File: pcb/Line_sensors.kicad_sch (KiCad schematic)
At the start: 23 parts, among them Q5 BC817, U10 CNY70, U11 CNY70, U5 CNY70, U6 CNY70, U7 CNY70, U8 CNY70, U9 CNY70

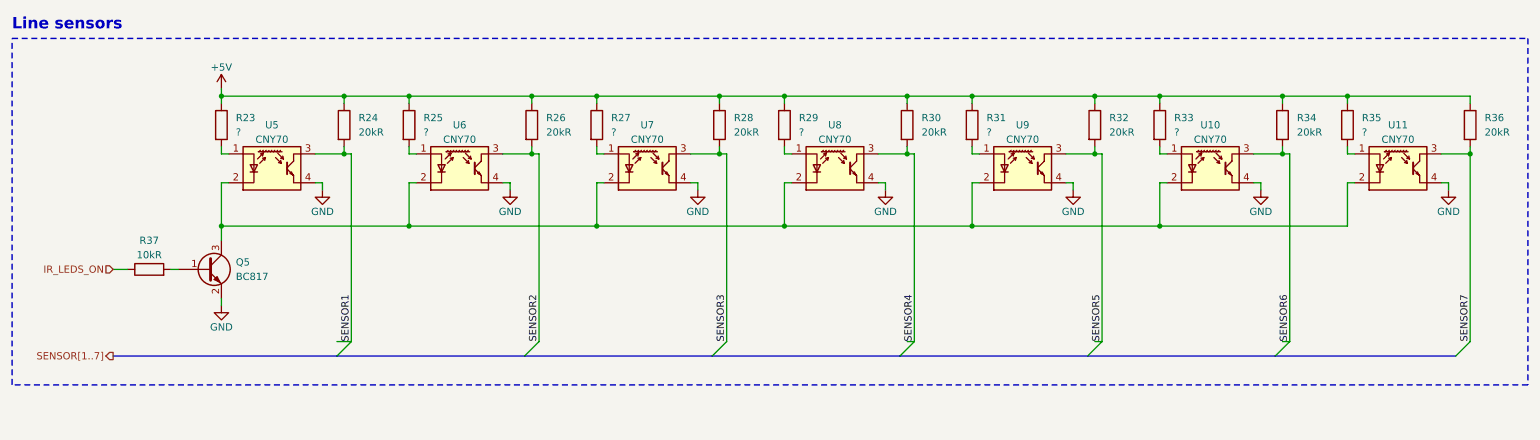
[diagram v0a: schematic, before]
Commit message: [pcb] Test point added
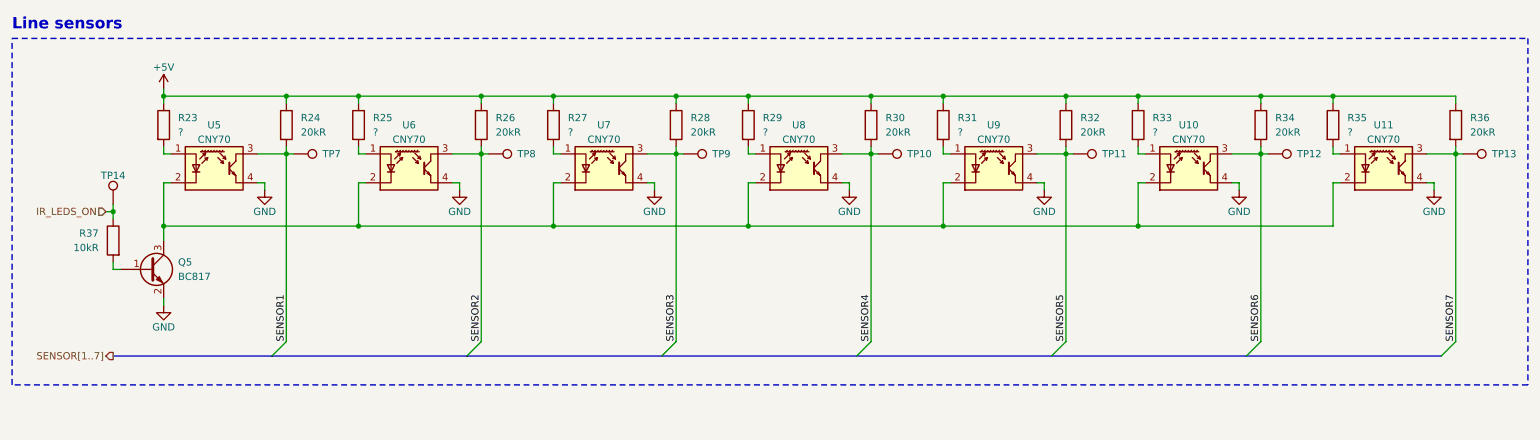
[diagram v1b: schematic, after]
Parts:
- added TP10, TP11, TP12, TP13, TP14, TP7, TP8, TP9: TestPoint, symbol Connector:TestPoint
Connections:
- net IR_LEDS_ON: now also TP14.1
- net SENSOR1: now also TP7.1
- net SENSOR2: now also TP8.1
- net SENSOR3: now also TP9.1
- net SENSOR4: now also TP10.1
- net SENSOR5: now also TP11.1
- net SENSOR6: now also TP12.1
- net SENSOR7: now also TP13.1
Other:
- moved on the sheet: Q5, R23, R24, R25, R26, R27, R28, R29, R30, R31, R32, R33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

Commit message: [pcb] Schematic clean-up
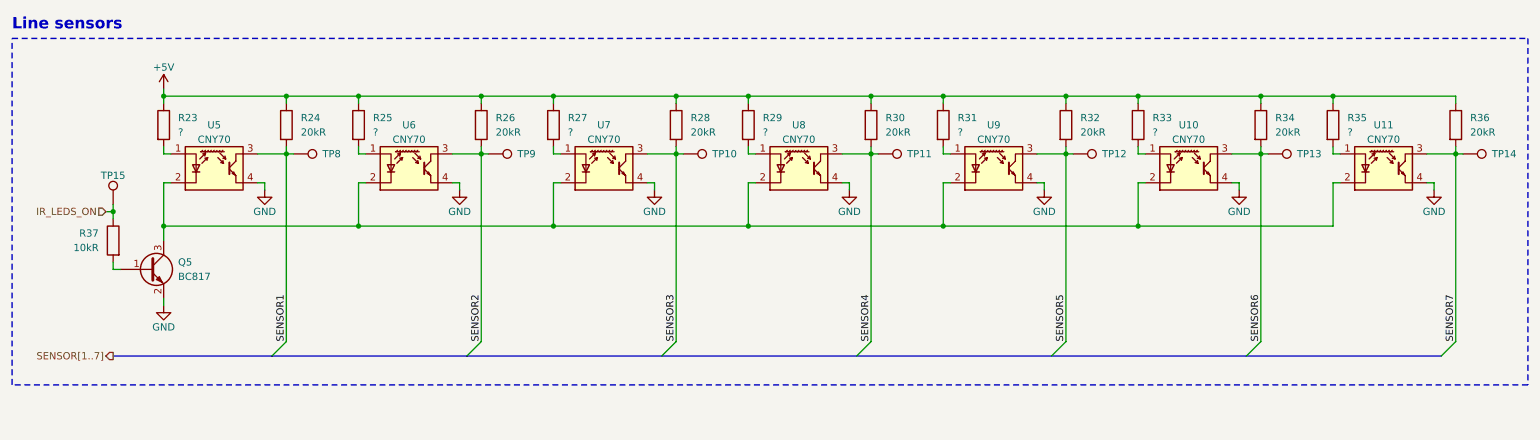
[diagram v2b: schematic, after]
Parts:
- renumbered TP9 to TP10, TP10 to TP11, TP11 to TP12, TP12 to TP13, TP13 to TP14, TP14 to TP15, TP7 to TP8, TP8 to TP9
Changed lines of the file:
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@@
   (symbol (lib_id "Connector:TestPoint") (at 236.22 39.37 270) (unit 1)
     (in_bom yes) (on_board yes) (dnp no)
-    (property "Reference" "TP12" (at 241.3 39.37 90)
+    (property "Reference" "TP13" (at 241.3 39.37 90)
       (effects (font (size 1.27 1.27)) (justify left))
     )
@@
       (project "Autko"
         (path "/8d5cfdec-de34-4148-9100-7125640c46f5/80d635c6-4a73-4538-989a-c930c6a7f33b"
-          (reference "TP12") (unit 1)
+          (reference "TP13") (unit 1)
         )
       )
@@
   (symbol (lib_id "Connector:TestPoint") (at 133.35 39.37 270) (unit 1)
     (in_bom yes) (on_board yes) (dnp no)
-    (property "Reference" "TP9" (at 138.43 39.37 90)
+    (property "Reference" "TP10" (at 138.43 39.37 90)
       (effects (font (size 1.27 1.27)) (justify left))
     )
@@
       (project "Autko"
         (path "/8d5cfdec-de34-4148-9100-7125640c46f5/80d635c6-4a73-4538-989a-c930c6a7f33b"
+          (reference "TP10") (unit 1)
+        )
+      )
+    )
+  )
+  (symbol (lib_id "Connector:TestPoint") (at 99.06 39.37 270) (unit 1)
+    (in_bom yes) (on_board yes) (dnp no)
+    (property "Reference" "TP9" (at 104.14 39.37 90)
+      (effects (font (size 1.27 1.27)) (justify left))
+    )
+    (property "Value" "TestPoint" (at 104.14 41.275 90)
+      (effects (font (size 1.27 1.27)) (justify left) hide)
+    )
+    (property "Footprint" "" (at 99.06 44.45 0)
+      (effects (font (size 1.27 1.27)) hide)
+    )
+    (property "Datasheet" "~" (at 99.06 44.45 0)
+      (effects (font (size 1.27 1.27)) hide)
+    )
+    (pin "1")
+    (instances
+      (project "Autko"
+        (path "/8d5cfdec-de34-4148-9100-7125640c46f5/80d635c6-4a73-4538-989a-c930c6a7f33b"
           (reference "TP9") (unit 1)
-        )
-      )
-    )
-  )
-  (symbol (lib_id "Connector:TestPoint") (at 99.06 39.37 270) (unit 1)
-    (in_bom yes) (on_board yes) (dnp no)
-    (property "Reference" "TP8" (at 104.14 39.37 90)
-      (effects (font (size 1.27 1.27)) (justify left))
-    )
-    (property "Value" "TestPoint" (at 104.14 41.275 90)
-      (effects (font (size 1.27 1.27)) (justify left) hide)
-    )
-    (property "Footprint" "" (at 99.06 44.45 0)
-      (effects (font (size 1.27 1.27)) hide)
-    )
-    (property "Datasheet" "~" (at 99.06 44.45 0)
-      (effects (font (size 1.27 1.27)) hide)
-    )
-    (pin "1")
-    (instances
-      (project "Autko"
-        (path "/8d5cfdec-de34-4148-9100-7125640c46f5/80d635c6-4a73-4538-989a-c930c6a7f33b"
-          (reference "TP8") (unit 1)
         )
       )
@@
   (symbol (lib_id "Connector:TestPoint") (at 201.93 39.37 270) (unit 1)
     (in_bom yes) (on_board yes) (dnp no)
-    (property "Reference" "TP11" (at 207.01 39.37 90)
+    (property "Reference" "TP12" (at 207.01 39.37 90)
       (effects (font (size 1.27 1.27)) (justify left))
     )
@@
       (project "Autko"
         (path "/8d5cfdec-de34-4148-9100-7125640c46f5/80d635c6-4a73-4538-989a-c930c6a7f33b"
-          (reference "TP11") (unit 1)
+          (reference "TP12") (unit 1)
         )
       )
@@
   (symbol (lib_id "Connector:TestPoint") (at 33.02 48.26 0) (unit 1)
     (in_bom yes) (on_board yes) (dnp no)
-    (property "Reference" "TP14" (at 33.02 43.18 0)
+    (property "Reference" "TP15" (at 33.02 43.18 0)
       (effects (font (size 1.27 1.27)))
     )
@@
       (project "Autko"
         (path "/8d5cfdec-de34-4148-9100-7125640c46f5/80d635c6-4a73-4538-989a-c930c6a7f33b"
-          (reference "TP14") (unit 1)
+          (reference "TP15") (unit 1)
         )
       )
@@
   (symbol (lib_id "Connector:TestPoint") (at 64.77 39.37 270) (unit 1)
     (in_bom yes) (on_board yes) (dnp no)
-    (property "Reference" "TP7" (at 69.85 39.37 90)
+    (property "Reference" "TP8" (at 69.85 39.37 90)
       (effects (font (size 1.27 1.27)) (justify left))
     )
@@
       (project "Autko"
         (path "/8d5cfdec-de34-4148-9100-7125640c46f5/80d635c6-4a73-4538-989a-c930c6a7f33b"
-          (reference "TP7") (unit 1)
+          (reference "TP8") (unit 1)
         )
       )
@@
   (symbol (lib_id "Connector:TestPoint") (at 270.51 39.37 270) (unit 1)
     (in_bom yes) (on_board yes) (dnp no)
-    (property "Reference" "TP13" (at 275.59 39.37 90)
+    (property "Reference" "TP14" (at 275.59 39.37 90)
       (effects (font (size 1.27 1.27)) (justify left))
     )
@@
       (project "Autko"
         (path "/8d5cfdec-de34-4148-9100-7125640c46f5/80d635c6-4a73-4538-989a-c930c6a7f33b"
-          (reference "TP13") (unit 1)
+          (reference "TP14") (unit 1)
         )
       )
@@
   (symbol (lib_id "Connector:TestPoint") (at 167.64 39.37 270) (unit 1)
     (in_bom yes) (on_board yes) (dnp no)
-    (property "Reference" "TP10" (at 172.72 39.37 90)
+    (property "Reference" "TP11" (at 172.72 39.37 90)
       (effects (font (size 1.27 1.27)) (justify left))
     )
@@
       (project "Autko"
         (path "/8d5cfdec-de34-4148-9100-7125640c46f5/80d635c6-4a73-4538-989a-c930c6a7f33b"
-          (reference "TP10") (unit 1)
-        )
-      )
+          (reference "TP11") (unit 1)
+        )
+      )

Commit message: [pcb] Footprints assigned
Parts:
- R23, R24, R25, R26, R27, R28, R29, R30, R31, R32, R33, R34, R35, R36, R37: footprint (none) -> Resistor_SMD:R_0805_2012Metric
- TP10, TP11, TP12, TP13, TP14, TP15, TP8, TP9: footprint (none) -> TestPoint:TestPoint_Pad_D2.0mm
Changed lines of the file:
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@@
       (effects (font (size 1.27 1.27)) (justify left))
     )
-    (property "Footprint" "" (at 34.798 54.61 90)
+    (property "Footprint" "Resistor_SMD:R_0805_2012Metric" (at 34.798 54.61 90)
       (effects (font (size 1.27 1.27)) hide)
     )
@@
       (effects (font (size 1.27 1.27)) (justify left))
     )
-    (property "Footprint" "" (at 245.872 34.29 90)
+    (property "Footprint" "Resistor_SMD:R_0805_2012Metric" (at 245.872 34.29 90)
       (effects (font (size 1.27 1.27)) hide)
     )
@@
       (effects (font (size 1.27 1.27)) (justify left))
     )
-    (property "Footprint" "" (at 143.002 34.29 90)
+    (property "Footprint" "Resistor_SMD:R_0805_2012Metric" (at 143.002 34.29 90)
       (effects (font (size 1.27 1.27)) hide)
     )
@@
       (effects (font (size 1.27 1.27)) (justify left) hide)
     )
-    (property "Footprint" "" (at 236.22 44.45 0)
+    (property "Footprint" "TestPoint:TestPoint_Pad_D2.0mm" (at 236.22 44.45 0)
       (effects (font (size 1.27 1.27)) hide)
     )
@@
       (effects (font (size 1.27 1.27)) (justify left) hide)
     )
-    (property "Footprint" "" (at 133.35 44.45 0)
+    (property "Footprint" "TestPoint:TestPoint_Pad_D2.0mm" (at 133.35 44.45 0)
       (effects (font (size 1.27 1.27)) hide)
     )
@@
       (effects (font (size 1.27 1.27)) (justify left) hide)
     )
-    (property "Footprint" "" (at 99.06 44.45 0)
+    (property "Footprint" "TestPoint:TestPoint_Pad_D2.0mm" (at 99.06 44.45 0)
       (effects (font (size 1.27 1.27)) hide)
     )
@@
       (effects (font (size 1.27 1.27)) (justify left))
     )
-    (property "Footprint" "" (at 40.132 34.29 90)
+    (property "Footprint" "Resistor_SMD:R_0805_2012Metric" (at 40.132 34.29 90)
       (effects (font (size 1.27 1.27)) hide)
     )
@@
       (effects (font (size 1.27 1.27)) (justify left))
     )
-    (property "Footprint" "" (at 61.722 34.29 90)
+    (property "Footprint" "Resistor_SMD:R_0805_2012Metric" (at 61.722 34.29 90)
       (effects (font (size 1.27 1.27)) hide)
     )
@@
       (effects (font (size 1.27 1.27)) (justify left))
     )
-    (property "Footprint" "" (at 74.422 34.29 90)
+    (property "Footprint" "Resistor_SMD:R_0805_2012Metric" (at 74.422 34.29 90)
       (effects (font (size 1.27 1.27)) hide)
     )
@@
       (effects (font (size 1.27 1.27)) (justify left))
     )
-    (property "Footprint" "" (at 108.712 34.29 90)
+    (property "Footprint" "Resistor_SMD:R_0805_2012Metric" (at 108.712 34.29 90)
       (effects (font (size 1.27 1.27)) hide)
     )
@@
       (effects (font (size 1.27 1.27)) (justify left))
     )
-    (property "Footprint" "" (at 164.592 34.29 90)
+    (property "Footprint" "Resistor_SMD:R_0805_2012Metric" (at 164.592 34.29 90)
       (effects (font (size 1.27 1.27)) hide)
     )
@@
       (effects (font (size 1.27 1.27)) (justify left))
     )
-    (property "Footprint" "" (at 233.172 34.29 90)
+    (property "Footprint" "Resistor_SMD:R_0805_2012Metric" (at 233.172 34.29 90)
       (effects (font (size 1.27 1.27)) hide)
     )
@@
       (effects (font (size 1.27 1.27)) (justify left))
     )
-    (property "Footprint" "" (at 177.292 34.29 90)
+    (property "Footprint" "Resistor_SMD:R_0805_2012Metric" (at 177.292 34.29 90)
       (effects (font (size 1.27 1.27)) hide)
     )
@@
       (effects (font (size 1.27 1.27)) (justify left) hide)
     )
-    (property "Footprint" "" (at 201.93 44.45 0)
+    (property "Footprint" "TestPoint:TestPoint_Pad_D2.0mm" (at 201.93 44.45 0)
       (effects (font (size 1.27 1.27)) hide)
     )
@@
       (effects (font (size 1.27 1.27)) (justify left) hide)
     )
-    (property "Footprint" "" (at 38.1 48.26 0)
+    (property "Footprint" "TestPoint:TestPoint_Pad_D2.0mm" (at 38.1 48.26 0)
       (effects (font (size 1.27 1.27)) hide)
     )
@@
       (effects (font (size 1.27 1.27)) (justify left))
     )
-    (property "Footprint" "" (at 96.012 34.29 90)
+    (property "Footprint" "Resistor_SMD:R_0805_2012Metric" (at 96.012 34.29 90)
       (effects (font (size 1.27 1.27)) hide)
     )
@@
       (effects (font (size 1.27 1.27)) (justify left) hide)
     )
-    (property "Footprint" "" (at 64.77 44.45 0)
+    (property "Footprint" "TestPoint:TestPoint_Pad_D2.0mm" (at 64.77 44.45 0)
       (effects (font (size 1.27 1.27)) hide)
     )
@@
       (effects (font (size 1.27 1.27)) (justify left))
     )
-    (property "Footprint" "" (at 198.882 34.29 90)
+    (property "Footprint" "Resistor_SMD:R_0805_2012Metric" (at 198.882 34.29 90)
       (effects (font (size 1.27 1.27)) hide)
     )
@@
       (effects (font (size 1.27 1.27)) (justify left))
     )
-    (property "Footprint" "" (at 211.582 34.29 90)
+    (property "Footprint" "Resistor_SMD:R_0805_2012Metric" (at 211.582 34.29 90)
       (effects (font (size 1.27 1.27)) hide)
     )
@@
       (effects (font (size 1.27 1.27)) (justify left) hide)
     )
-    (property "Footprint" "" (at 270.51 44.45 0)
+    (property "Footprint" "TestPoint:TestPoint_Pad_D2.0mm" (at 270.51 44.45 0)
       (effects (font (size 1.27 1.27)) hide)
     )
@@
       (effects (font (size 1.27 1.27)) (justify left) hide)
     )
-    (property "Footprint" "" (at 167.64 44.45 0)
+    (property "Footprint" "TestPoint:TestPoint_Pad_D2.0mm" (at 167.64 44.45 0)
       (effects (font (size 1.27 1.27)) hide)
     )
@@
       (effects (font (size 1.27 1.27)) (justify left))
     )
-    (property "Footprint" "" (at 267.462 34.29 90)
+    (property "Footprint" "Resistor_SMD:R_0805_2012Metric" (at 267.462 34.29 90)
       (effects (font (size 1.27 1.27)) hide)
     )
@@
       (effects (font (size 1.27 1.27)) (justify left))
     )
-    (property "Footprint" "" (at 130.302 34.29 90)
-      (effects (font (size 1.27 1.27)) hide)
-    )
+    (property "Footprint" "Resistor_SMD:R_0805_2012Metric" (at 130.302 34.29 90)
+      (effects (font (size 1.27 1.27)) hide)
+    )

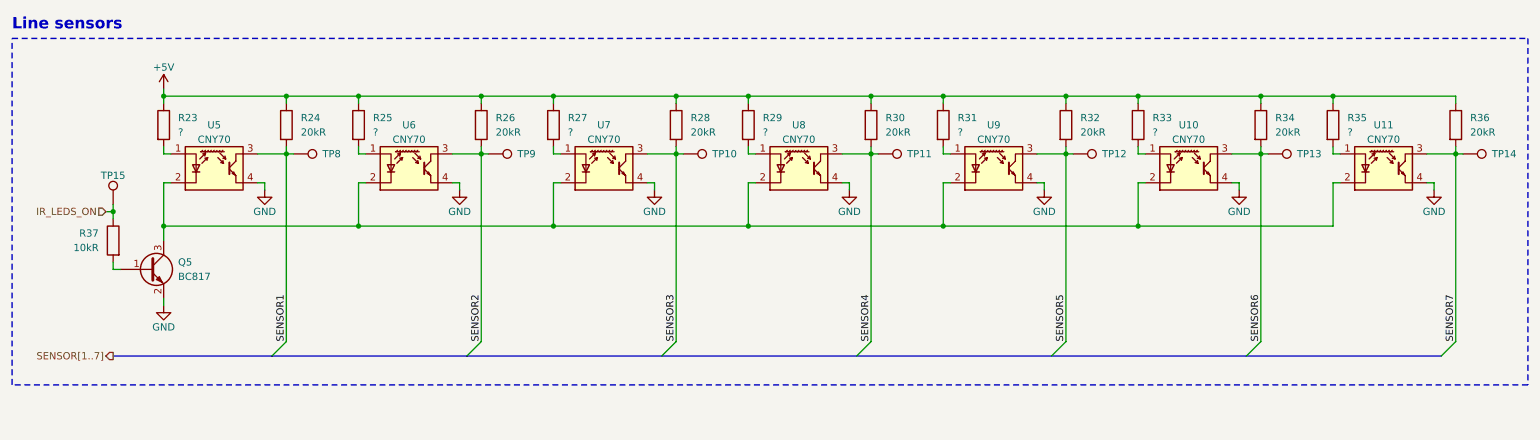
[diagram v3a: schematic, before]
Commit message: [pcb] Rework schematic for ATxmega16A4U
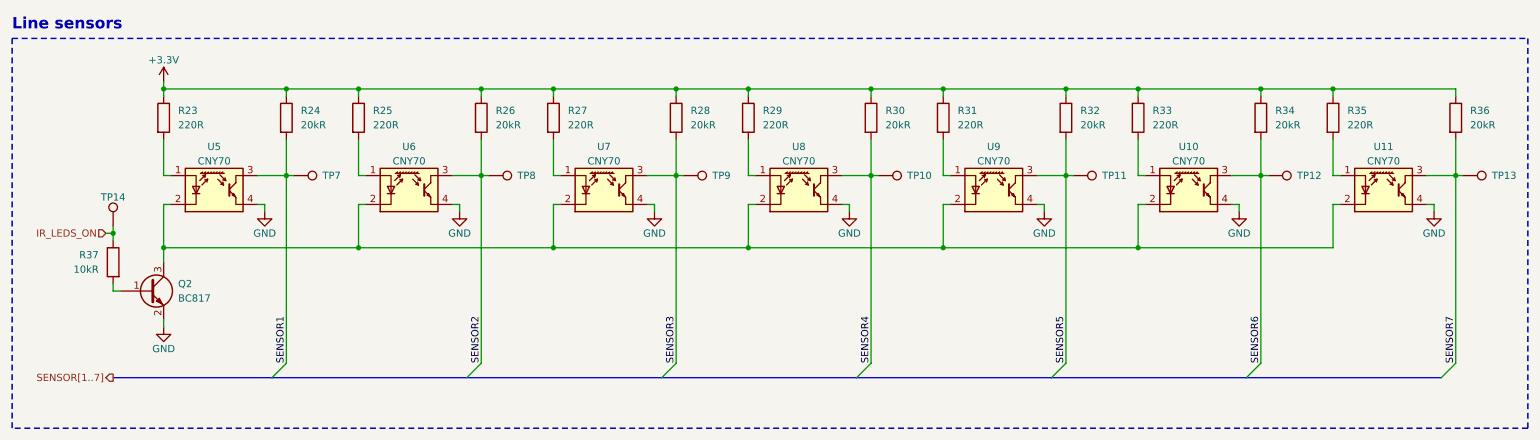
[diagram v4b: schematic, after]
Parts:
- R23, R25, R27, R29, R31, R33, R35: value ? -> 220R
- renumbered Q5 to Q2, TP11 to TP10, TP12 to TP11, TP13 to TP12, TP14 to TP13, TP15 to TP14, TP8 to TP7, TP9 to TP8, TP10 to TP9
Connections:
- net +5V renamed +3.3V
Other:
- moved on the sheet: Q2, R23, R24, R25, R26, R27, R28, R29, R30, R31, R32, R33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
